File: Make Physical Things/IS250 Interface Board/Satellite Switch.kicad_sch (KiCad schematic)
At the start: 3 parts, among them SW3 SW_MEC_5G, SW4 SW_MEC_5G, SW5 SW_MEC_5G

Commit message: Updated Components to have footprints
Added footprints to components that had the wrong ones or were completely missing
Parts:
- SW3, SW4, SW5: footprint (none) -> Button_Switch_THT:SW_Tactile_SPST_Angled_PTS645Vx58-2LFS
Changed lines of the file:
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@@
     (property "Reference" "SW4" (id 0) (at 100.838 69.85 0))
     (property "Value" "SW_MEC_5G" (id 1) (at 100.838 72.39 0))
-    (property "Footprint" "" (id 2) (at 100.838 72.39 0)
+    (property "Footprint" "Button_Switch_THT:SW_Tactile_SPST_Angled_PTS645Vx58-2LFS" (id 2) (at 100.838 72.39 0)
       (effects (font (size 1.27 1.27)) hide)
     )
@@
     (property "Reference" "SW5" (id 0) (at 100.838 80.01 0))
     (property "Value" "SW_MEC_5G" (id 1) (at 100.838 82.55 0))
-    (property "Footprint" "" (id 2) (at 100.838 82.55 0)
+    (property "Footprint" "Button_Switch_THT:SW_Tactile_SPST_Angled_PTS645Vx58-2LFS" (id 2) (at 100.838 82.55 0)
       (effects (font (size 1.27 1.27)) hide)
     )
@@
     (property "Reference" "SW3" (id 0) (at 100.838 59.69 0))
     (property "Value" "SW_MEC_5G" (id 1) (at 100.838 62.23 0))
-    (property "Footprint" "" (id 2) (at 100.838 62.23 0)
+    (property "Footprint" "Button_Switch_THT:SW_Tactile_SPST_Angled_PTS645Vx58-2LFS" (id 2) (at 100.838 62.23 0)
       (effects (font (size 1.27 1.27)) hide)
     )

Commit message: Added Reset Circuit
Added a button to allow you to reset the arduino, if it decides to die. Also fixed the footprints for the buttons so that they actually function as buttons.
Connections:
- net GND: now also SW3.1 (A), SW3.2 (A), SW4.1 (A), SW4.2 (A), SW5.1 (A), SW5.2 (A); no longer SW3.3 (B), SW3.4 (B), SW4.3 (B), SW4.4 (B), SW5.3 (B), SW5.4 (B)
- net LSEL: now also SW5.4 (B); no longer SW5.1 (A)
- net RSEL: now also SW3.4 (B); no longer SW3.1 (A)
- net SET: now also SW4.4 (B); no longer SW4.1 (A)
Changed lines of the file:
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@@
     (effects (font (size 1.27 1.27)) (justify right))
   )
-  (symbol (lib_id "Switch:SW_MEC_5G") (at 100.838 77.47 0) (unit 1)
+  (symbol (lib_name "SW_MEC_5G_2") (lib_id "Switch:SW_MEC_5G") (at 100.838 77.47 0) (mirror y) (unit 1)
     (in_bom yes) (on_board yes) (fields_autoplaced)
     (property "Reference" "SW4" (id 0) (at 100.838 69.85 0))
@@
     )
     (pin "1")
-    (pin "3")
+    (pin "2")
     (pin "2")
     (pin "4")
@@
     (pin "1")
   )
-  (symbol (lib_id "Switch:SW_MEC_5G") (at 100.838 87.63 0) (unit 1)
+  (symbol (lib_id "Switch:SW_MEC_5G") (at 100.838 87.63 0) (mirror y) (unit 1)
     (in_bom yes) (on_board yes) (fields_autoplaced)
     (property "Reference" "SW5" (id 0) (at 100.838 80.01 0))
@@
     )
     (pin "1")
-    (pin "3")
+    (pin "2")
     (pin "2")
     (pin "4")
   )
-  (symbol (lib_id "Switch:SW_MEC_5G") (at 100.838 67.31 0) (unit 1)
+  (symbol (lib_name "SW_MEC_5G_1") (lib_id "Switch:SW_MEC_5G") (at 100.838 67.31 0) (mirror y) (unit 1)
     (in_bom yes) (on_board yes) (fields_autoplaced)
     (property "Reference" "SW3" (id 0) (at 100.838 59.69 0))
@@
     )
     (pin "1")
-    (pin "3")
+    (pin "2")
     (pin "2")
     (pin "4")

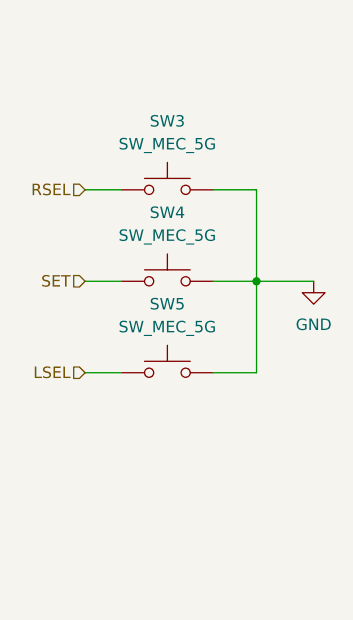
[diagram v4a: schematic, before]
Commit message: PCB Layout Finalised
Finalised the layout, routing and silkscreen still to be completed.
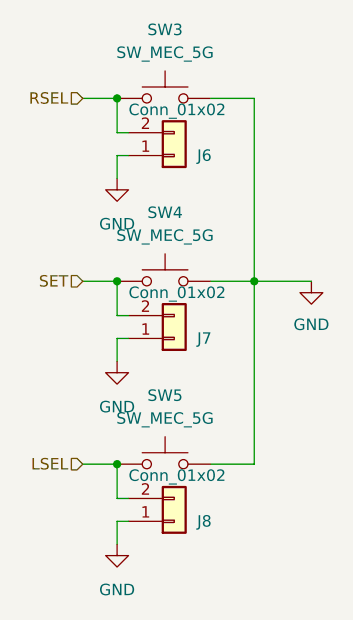
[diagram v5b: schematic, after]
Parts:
- added J6, J7, J8: Conn_01x02, Connector_PinHeader_2.54mm:PinHeader_1x02_P2.54mm_Vertical, symbol Connector_Generic:Conn_01x02
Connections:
- net GND: now also J6.1 (Pin_1), J7.1 (Pin_1), J8.1 (Pin_1)
- net LSEL: now also J8.2 (Pin_2)
- net RSEL: now also J6.2 (Pin_2)
- net SET: now also J7.2 (Pin_2)
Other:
- moved on the sheet: SW3, SW5
